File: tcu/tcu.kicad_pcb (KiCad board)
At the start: 2 copper layers, 52 parts, among them CON1 USB-MICRO-B, K1 SPDT_RELAY, K2 SPDT_RELAY, K3 SPDT_RELAY, P1 CONN_01X08, P2 CONN_02X03, P3 NRF24L01+, P4 ESP8266, Q1 E_NMOS, Q2 E_NMOS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

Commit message: ALL ROUTING COMPLETE
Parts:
- moved P3 47.1 mm to (120.4, 66.0), turned to 270 degrees
- moved P4 45.3 mm to (138.7, 24.6), turned to 0 degrees
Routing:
- net GND: track 322.3 -> 434.2 mm, vias 14 -> 19
- net VCC: track 196.7 -> 295.7 mm, vias 10 -> 19
- net /BACKLIGHT: track 1.24 -> 49.1 mm, vias 1 -> 0
- net /ESP_RESET: track 53.1 -> 99.6 mm
- net /CE: track 4.51 -> 51.1 mm, vias 1 -> 2
- net /CSN: track 5.16 -> 47.2 mm, vias 1 -> 2
- net /RELAY2: track 0.00 -> 40.7 mm, vias 0 -> 2
- net /CH_PD: track 66.3 -> 103.8 mm, vias 5 -> 4
- net /SCK: track 43.6 -> 79.1 mm, vias 3 -> 6
- net /MOSI: track 59.2 -> 90.6 mm, vias 6 -> 8
- net /RXD: track 43.1 -> 70.3 mm, vias 2 -> 3
- net /GPIO0: track 45.1 -> 71.7 mm, vias 2 -> 3
- net /GPIO2: track 55.0 -> 78.6 mm, vias 2 -> 3
- net /MISO: track 58.3 -> 80.4 mm
- net /TXD: track 64.6 -> 78.9 mm
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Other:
- board text added: "M.R. THERMOSTAT TCU TYLER BULES JACOB STURM CHRIS FASTBINDER"

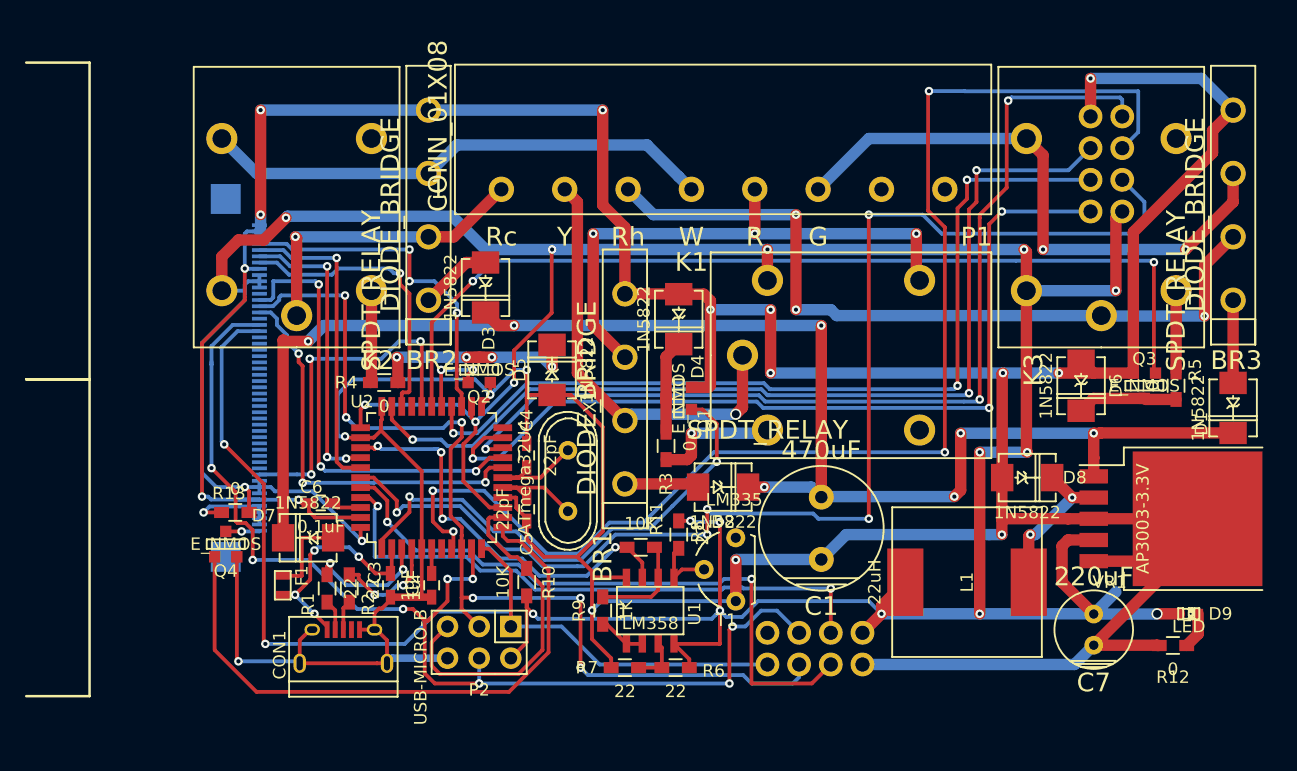
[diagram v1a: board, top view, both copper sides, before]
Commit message: normalized fonts and aligned references
also rerouted backlight trace
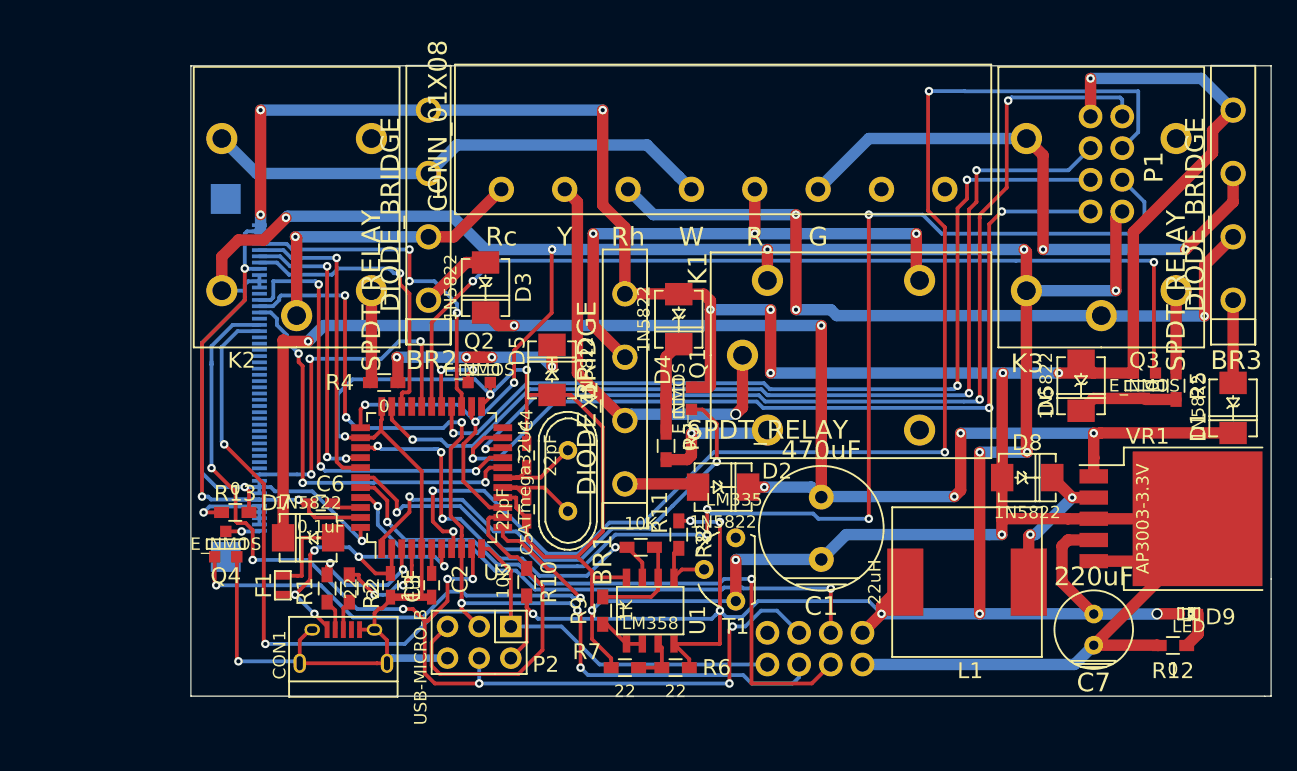
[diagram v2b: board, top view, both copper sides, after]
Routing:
- net /UVCC: track 18.6 -> 27.3 mm, vias 4 -> 5
- net /BACKLIGHT: track 49.1 -> 42.7 mm, vias 0 -> 2
- net VCC: track 295.7 -> 293.2 mm
- net /CSN: track 47.2 -> 45.3 mm
- net /SCK: track 79.1 -> 78.2 mm
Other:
- board outline added: 86.6 x 50.5 mm

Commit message: fixed fastbinder to fasbinder
new gerbers generated and packaged. sending for quote.
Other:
- board text added: "M.R. THERMOSTAT TCU TYLER BULES JACOB STURM CHRIS FASBINDER"
- board text removed: "M.R. THERMOSTAT TCU TYLER BULES JACOB STURM CHRIS FASTBINDER"
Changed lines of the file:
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@@
     (links 159)
     (no_connects 0)
-    (area 53.239999 17.8972 155.247372 72.3428)
+    (area 66.160629 17.8972 155.247372 72.3428)
     (thickness 1.6)
     (drawings 7)
@@
   (gr_line (start 66.548 71.12) (end 152.654 71.12) (layer Edge.Cuts) (width 0.1))
   (gr_line (start 66.548 20.574) (end 66.548 71.12) (layer Edge.Cuts) (width 0.1))
-  (gr_text "M.R. THERMOSTAT TCU\nTYLER BULES\nJACOB STURM\nCHRIS FASTBINDER" (at 152.146 56.896) (layer B.SilkS)
+  (gr_text "M.R. THERMOSTAT TCU\nTYLER BULES\nJACOB STURM\nCHRIS FASBINDER" (at 152.146 56.896) (layer B.SilkS)
     (effects (font (size 1.5 1.5) (thickness 0.3)) (justify left mirror))
   )
